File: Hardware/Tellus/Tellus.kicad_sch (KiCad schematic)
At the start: 34 parts, among them J1 Conn_01x10_Female, M1 Motor_DC, M2 Motor_DC, M3 Motor_DC, M4 Motor_DC, M5 Motor_DC, M6 Motor_DC, U1 AMS1117-3.3, U2 ICM-42670-P, U3 MAX8815A, U4 MC6470, U5 LM7805_TO220, U6 A3909, U7 A3909, U8 A3909, U9 DEV-16771

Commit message: Add files via upload
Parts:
- removed R4: 100K, symbol Device:R
- added BT1: Battery_Cell, symbol Device:Battery_Cell
- added J2: Conn_01x06_Female, symbol Connector:Conn_01x06_Female
- added J3: Conn_01x04_Female, symbol Connector:Conn_01x04_Female
- added J4: Conn_01x02_Female, symbol Connector:Conn_01x02_Female
- R3: value 300K -> 10K
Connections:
- net 3.3V: now also R3.1; no longer U9.VIN
- net 5V: now also U9.VIN, J3.3 (Pin_3)
- net Battery Output: now also J2.1 (Pin_1)
- net GND: now also J2.6 (Pin_6), J3.4 (Pin_4), J4.2 (Pin_2); no longer C7.1, R1.2, R3.2, U3.6 (FB), U3.7 (OUTS)
- net SCLK: now also J3.1 (Pin_1)
- net SDA: now also J3.2 (Pin_2)
- net at C8.1, R1.1, U3.10_9 (POUT)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: now also U3.6 (FB); no longer R3.1
- net LDR Out: now reaches U9.20 (A6)
- net LDR Out: now also R3.2, J4.1 (Pin_1)
- new net: BT1.1 (+), J2.3 (Pin_3)
- new net: BT1.2 (-), J2.4 (Pin_4)
- new net: C7.1, R1.2, U3.7 (OUTS)
- no-connect marks 37 -> 38
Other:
- note added: "Battery Charger Breakout"
- note added: "LDR Breakout"
- note added: "LiDAR Breakout"
- moved on the sheet: C1, C10, C11, C2, C3, C4, C5, C6, C7, C8, C9, J1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

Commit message: Add files via upload
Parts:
- removed BT1: Battery_Cell, symbol Device:Battery_Cell
- removed C4: 10uF, symbol Device:C
- removed C7: 0.1uF, symbol Device:C
- removed C8, C9: 22uF, symbol Device:C
- removed J1: Conn_01x10_Female, symbol Connector:Conn_01x10_Female
- removed J2: Conn_01x06_Female, symbol Connector:Conn_01x06_Female
- removed J3: Conn_01x04_Female, symbol Connector:Conn_01x04_Female
- removed L1: 2u, symbol Device:L
- removed M1, M2, M3, M4, M5, M6: Motor_DC, symbol Motor:Motor_DC
- removed R1: 100, symbol Device:R
- removed U3: MAX8815A, symbol BoostConverter:MAX8815A
- removed U5: LM7805_TO220, Package_TO_SOT_THT:TO-220-3_Vertical, symbol Regulator_Linear:LM7805_TO220
- added C5, C6: 22uF, Capacitor_SMD:C_1210_3225Metric_Pad1.33x2.70mm_HandSolder, symbol Device:C
- added J1, J10, J2, J3, J4, J5, J7, J8, J9: Conn_01x02_Female, Connector_PinHeader_2.54mm:PinHeader_1x02_P2.54mm_Vertical, symbol Connector:Conn_01x02_Female
- added J11, J12: Conn_01x04_Female, Connector_PinHeader_2.00mm:PinHeader_1x04_P2.00mm_Vertical, symbol Connector:Conn_01x04_Female
- added J13, J14: Conn_01x03_Female, Connector_PinHeader_2.00mm:PinHeader_1x03_P2.00mm_Vertical, symbol Connector:Conn_01x03_Female
- C1: renamed from C11; value 66uF -> 22uF; footprint (none) -> Capacitor_SMD:C_1210_3225Metric_Pad1.33x2.70mm_HandSolder
- C2: renamed from C5; footprint (none) -> Capacitor_SMD:C_1210_3225Metric_Pad1.33x2.70mm_HandSolder
- C3: renamed from C2; footprint (none) -> Capacitor_SMD:C_1210_3225Metric_Pad1.33x2.70mm_HandSolder
- C4: renamed from C1; footprint (none) -> Capacitor_SMD:C_1210_3225Metric_Pad1.33x2.70mm_HandSolder
- C7: renamed from C6; footprint (none) -> Capacitor_SMD:C_1210_3225Metric_Pad1.33x2.70mm_HandSolder
- C8: renamed from C3; footprint (none) -> Capacitor_SMD:C_1210_3225Metric_Pad1.33x2.70mm_HandSolder
- C9: renamed from C10; footprint (none) -> Capacitor_SMD:C_1210_3225Metric_Pad1.33x2.70mm_HandSolder
- J6: renamed from J4; footprint (none) -> Connector_PinHeader_2.54mm:PinHeader_1x02_P2.54mm_Vertical
- R1: renamed from R3; footprint (none) -> Resistor_SMD:R_1206_3216Metric
- R2: renamed from R5; footprint (none) -> Resistor_SMD:R_1206_3216Metric
- R3: renamed from R6; footprint (none) -> Resistor_SMD:R_1206_3216Metric
- R4: renamed from R2; footprint (none) -> Resistor_SMD:R_1206_3216Metric
- U1: renamed from U8; footprint (none) -> Package_SO:MSOP-10-1EP_3x3mm_P0.5mm_EP1.73x1.98mm_ThermalVias
- U3: renamed from U7; footprint (none) -> Package_SO:MSOP-10-1EP_3x3mm_P0.5mm_EP1.73x1.98mm_ThermalVias
- U4: renamed from U6; footprint (none) -> Package_SO:MSOP-10-1EP_3x3mm_P0.5mm_EP1.73x1.98mm_ThermalVias
- U5: renamed from U9; footprint MODULE_DEV-16771 -> KicadLibs:MODULE_DEV-16771
- U6: renamed from U4; footprint PQFN50P200X200X100-12N -> KicadLibs:PQFN50P200X200X100-12N
- U7: renamed from U2; footprint IC_ICM-42670-P -> ICM42670P:IC_ICM-42670-P
- renumbered U1 to U2
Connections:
- net Battery Output is gone; now on net 5V: C8.2, U2.3 (VI)
- net 3.3V: now also J12.4 (Pin_4)
- net 5V: now also C5.1, C6.1, J10.1 (Pin_1), J8.1 (Pin_1), J9.1 (Pin_1)
- net FSYNC_ICM: now also U5.33 (MCLK2); no longer U5.31 (CTX3)
- net Front Left Control 1: now also U5.17 (A3); no longer U5.14 (A0)
- net Front Left Control 2: now also U5.16 (A2); no longer U5.15 (A1)
- net Front Right Control 1: now also U5.15 (A1); no longer U5.16 (A2)
- net Front Right Control 2: now also U5.14 (A0); no longer U5.17 (A3)
- net GND: now also C5.2, C6.2, J10.2 (Pin_2), J11.3 (Pin_3), J12.1 (Pin_1), J13.2 (Pin_2), J13.3 (Pin_3), J8.2 (Pin_2), J9.2 (Pin_2)
- net INT1_ICM: now also U5.22 (A8); no longer U5.7 (RX2)
- net INT2_ICM: now also U5.37 (CS3); no longer U5.8 (TX2)
- net INT_BT: now also J13.1 (Pin_1)
- net PDN: now also J12.2 (Pin_2)
- net RXD: now also J11.1 (Pin_1)
- net Rear Left Control 1: now also U5.41 (A17); no longer U5.38 (A14)
- net Rear Left Control 2: now also U5.40 (A16); no longer U5.39 (A15)
- net Rear Right Control 1: now also U5.39 (A15); no longer U5.40 (A16)
- net Rear Right Control 2: now also U5.38 (A14); no longer U5.41 (A17)
- net TXD: now also J11.2 (Pin_2)
- net WAKEUP: now also J12.3 (Pin_3)
- net at U1.10 (OUT_1): now also J1.1 (Pin_1)
- net at U1.6 (OUT_4): now also J2.2 (Pin_2)
- net at U1.7 (OUT_3): now also J2.1 (Pin_1)
- net at U1.9 (OUT_2): now also J1.2 (Pin_2)
- net at U3.10 (OUT_1): now also J4.1 (Pin_1)
- net at U3.9 (OUT_2): now also J4.2 (Pin_2)
- net at U4.7 (OUT_3): now also J7.1 (Pin_1)
- net at U4.6 (OUT_4): now also J7.2 (Pin_2)
- net at U4.10 (OUT_1): now also J5.1 (Pin_1)
- net at U4.9 (OUT_2): now also J5.2 (Pin_2)
- net Lidar_PWM: now reaches U5.23 (A9)
- net Lidar_PWM: now also J14.3 (Pin_3)
- net at U3.6 (OUT_4): now also J3.2 (Pin_2)
- net at U3.7 (OUT_3): now also J3.1 (Pin_1)
- new net Lidar_RX: J14.2 (Pin_2), U5.7 (RX2)
- new net Lidar_TX: J14.1 (Pin_1), U5.8 (TX2)
- no-connect marks 38 -> 34
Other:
- note removed: "Battery Charger Breakout"
- moved on the sheet: C1, C2, C4, C7, C9, R4, U6, U7

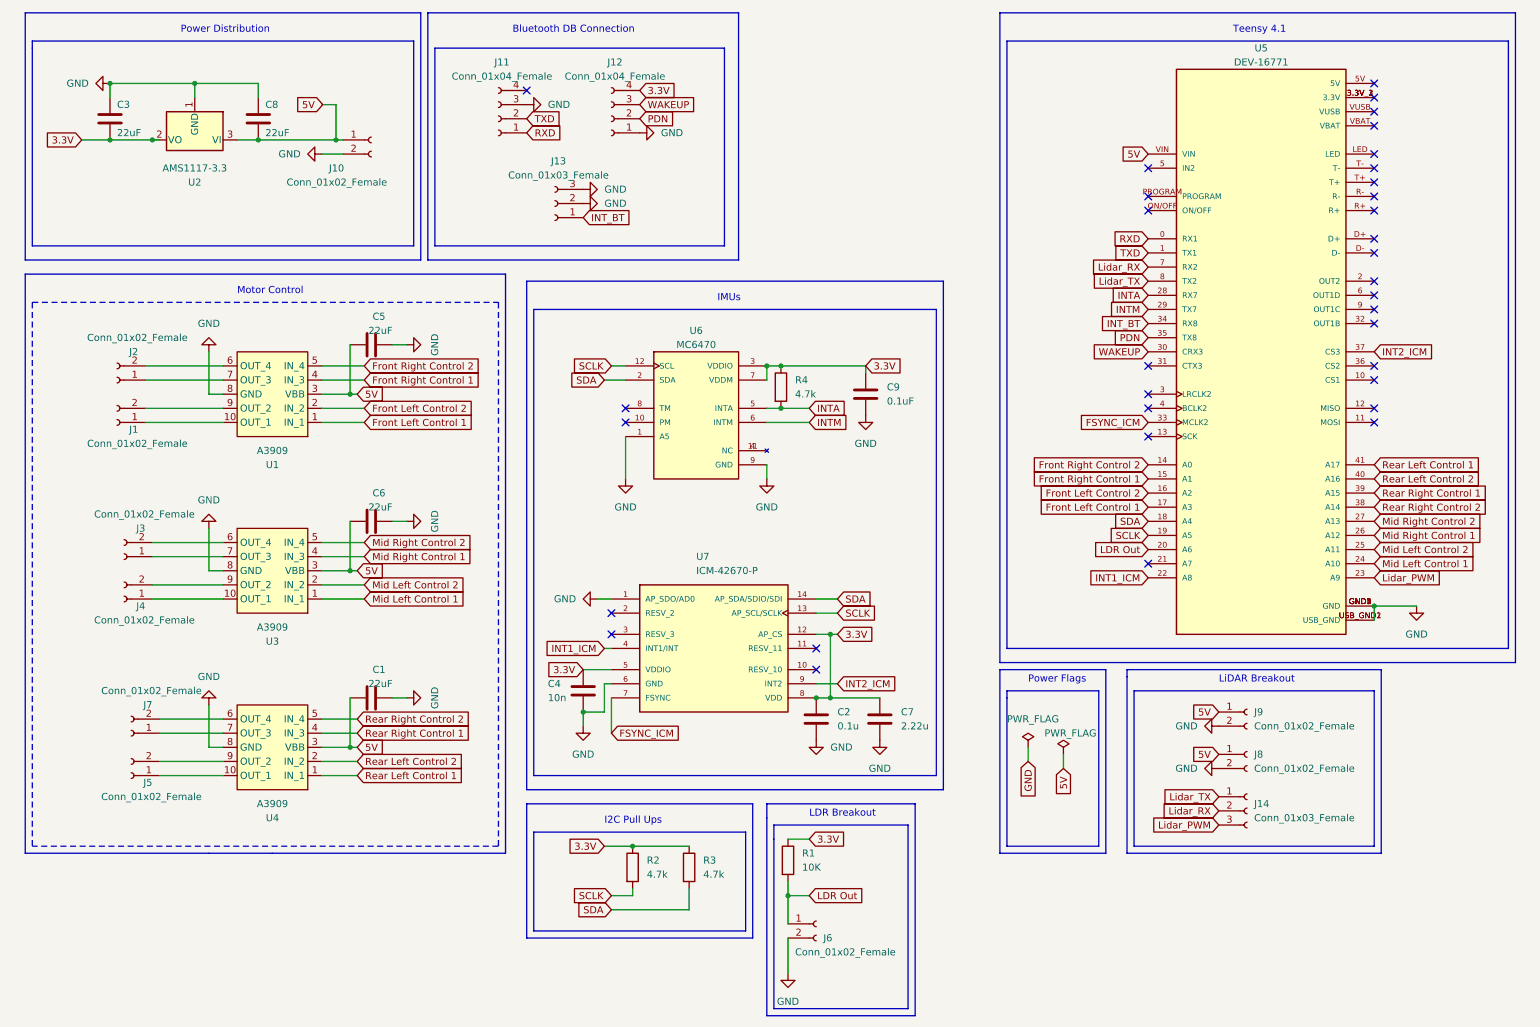
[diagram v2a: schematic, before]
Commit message: PCB Updates
Re-Layered PCB to match Signal, PWR, GND, Signal suggestion. Cleaned up power connections, Bluetooth saddle, and LiDAR mounts.

Fixed the following DRC Violations/Warnings:
No Footprint assigned for Mounting holes
- Fixed by adding them in the schematic.

Unconnected 3.3V Terminals on Teensy
- Fixed Symbol in schematic that had them on top of each other. The teensy spec does not recommend tying these together.

No net assigned for Motor Driver EP
-Modified Symbol in schematic to include the EP, and connected it to GND, as suggested in the data sheet.
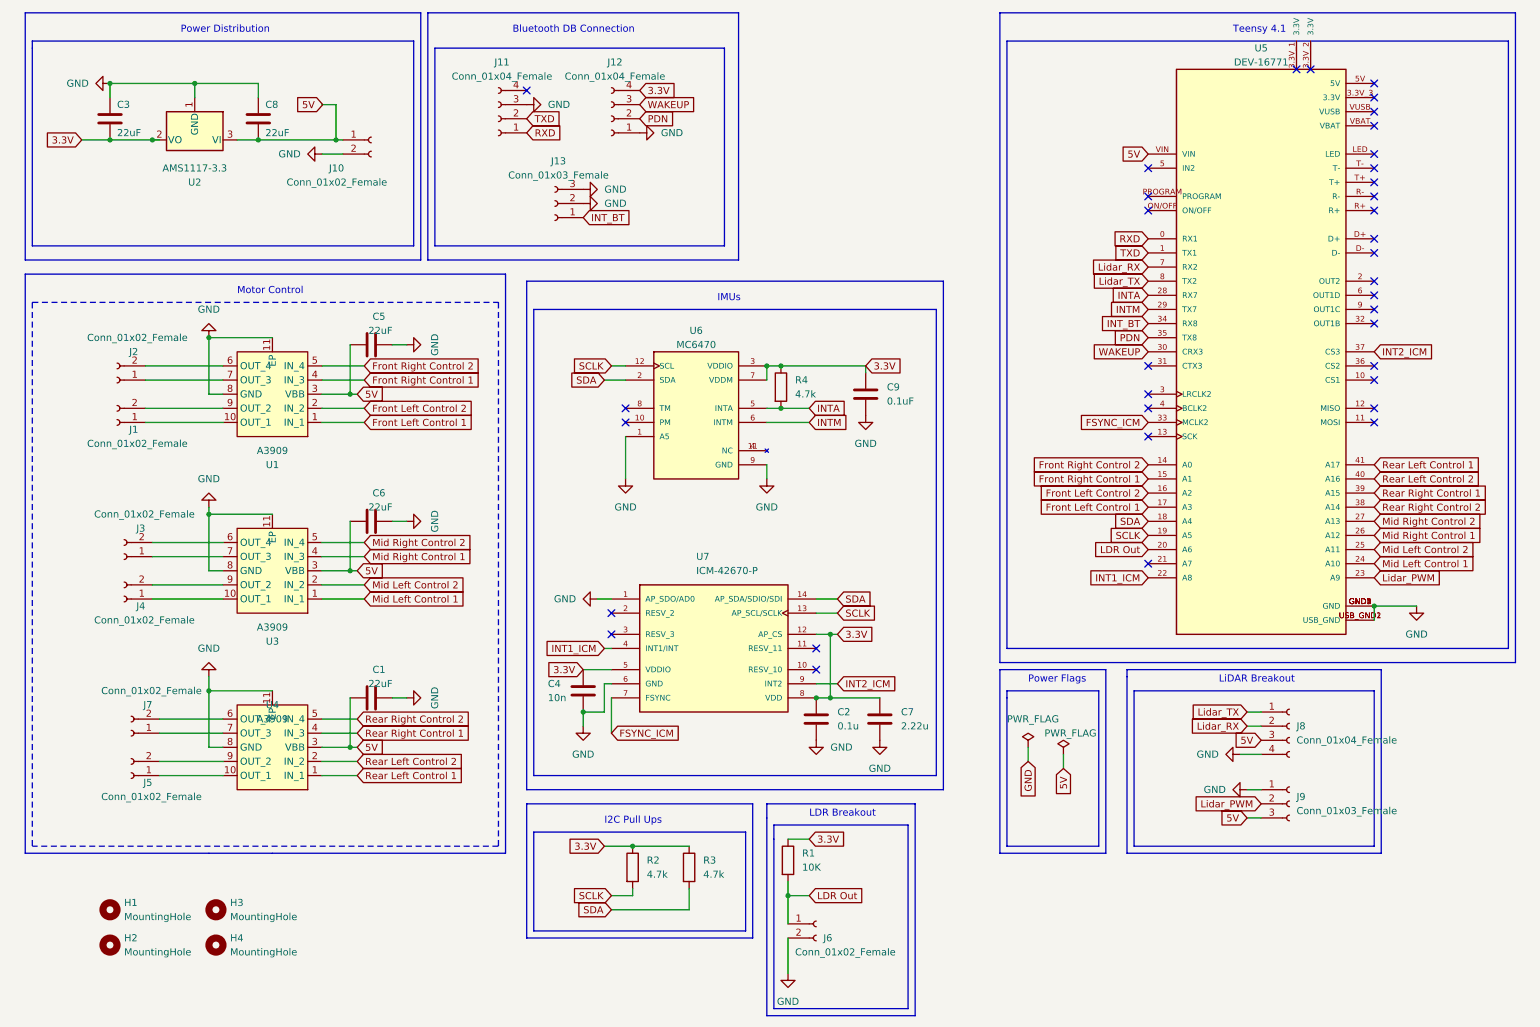
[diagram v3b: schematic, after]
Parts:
- removed J14: Conn_01x03_Female, Connector_PinHeader_2.00mm:PinHeader_1x03_P2.00mm_Vertical, symbol Connector:Conn_01x03_Female
- removed J8, J9: Conn_01x02_Female, Connector_PinHeader_2.54mm:PinHeader_1x02_P2.54mm_Vertical, symbol Connector:Conn_01x02_Female
- added H1, H2, H3, H4: MountingHole, symbol Mechanical:MountingHole
- added J8: Conn_01x04_Female, Connector_PinHeader_2.54mm:PinHeader_1x04_P2.54mm_Vertical, symbol Connector:Conn_01x04_Female
- added J9: Conn_01x03_Female, Connector_PinHeader_2.54mm:PinHeader_1x03_P2.54mm_Vertical, symbol Connector:Conn_01x03_Female
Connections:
- net 5V: now also J8.3 (Pin_3), J9.3 (Pin_3)
- net GND: now also U1.11 (EP), U3.11 (EP), U4.11 (EP), J8.4 (Pin_4), J9.1 (Pin_1)
- net Lidar_PWM: now also J9.2 (Pin_2)
- net Lidar_RX: now also J8.2 (Pin_2)
- net Lidar_TX: now also J8.1 (Pin_1)
- now unconnected: U5.3.3V_1 (3.3V), U5.3.3V_2 (3.3V), U5.3.3V_3 (3.3V)
- no-connect marks 34 -> 36

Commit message: Final Edits and Manufacturer File Generation
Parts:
- C2: value 0.1u -> 0.1uF
- C7: value 2.22u -> 2.22uF
- U1, U3, U4: footprint Package_SO:MSOP-10-1EP_3x3mm_P0.5mm_EP1.73x1.98mm_ThermalVias -> Package_SO:SSOP-10_3.9x4.9mm_P1.00mm
- U2: footprint Package_TO_SOT_SMD:SOT-223-3_TabPin2 -> Package_TO_SOT_SMD:SOT-89-3
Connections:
- net GND: no longer U1.11 (EP), U3.11 (EP), U4.11 (EP)
- net at U6.11 (NC): no longer U6.4 (NC)
